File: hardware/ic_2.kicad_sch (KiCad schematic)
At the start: 24 parts, among them IC3 BTS722204ESAXUMA1

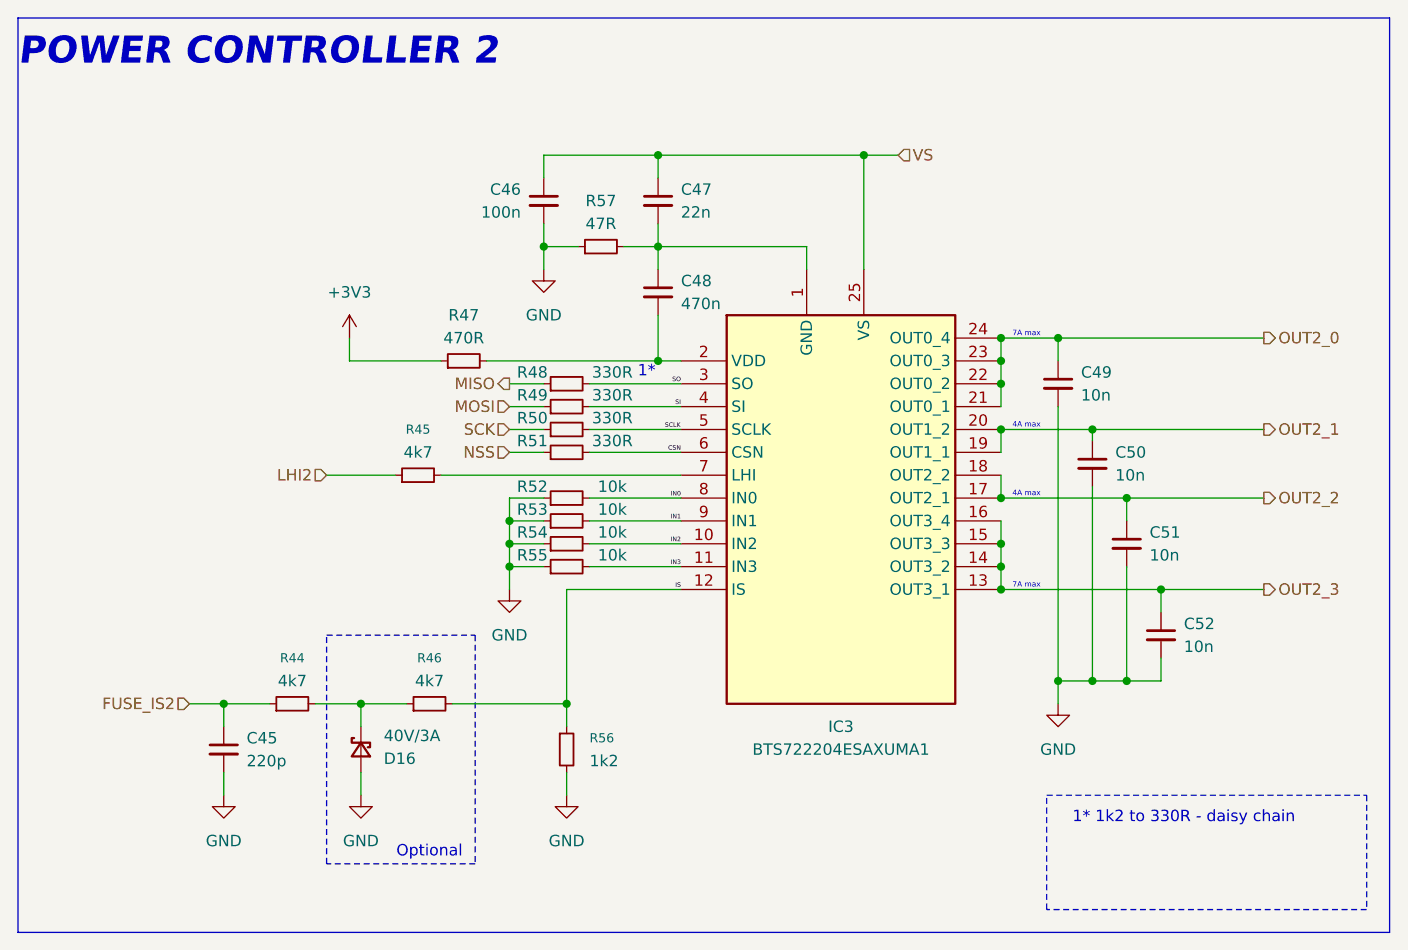
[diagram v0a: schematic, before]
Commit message: new pcb layout & can coppied from steeringwheel
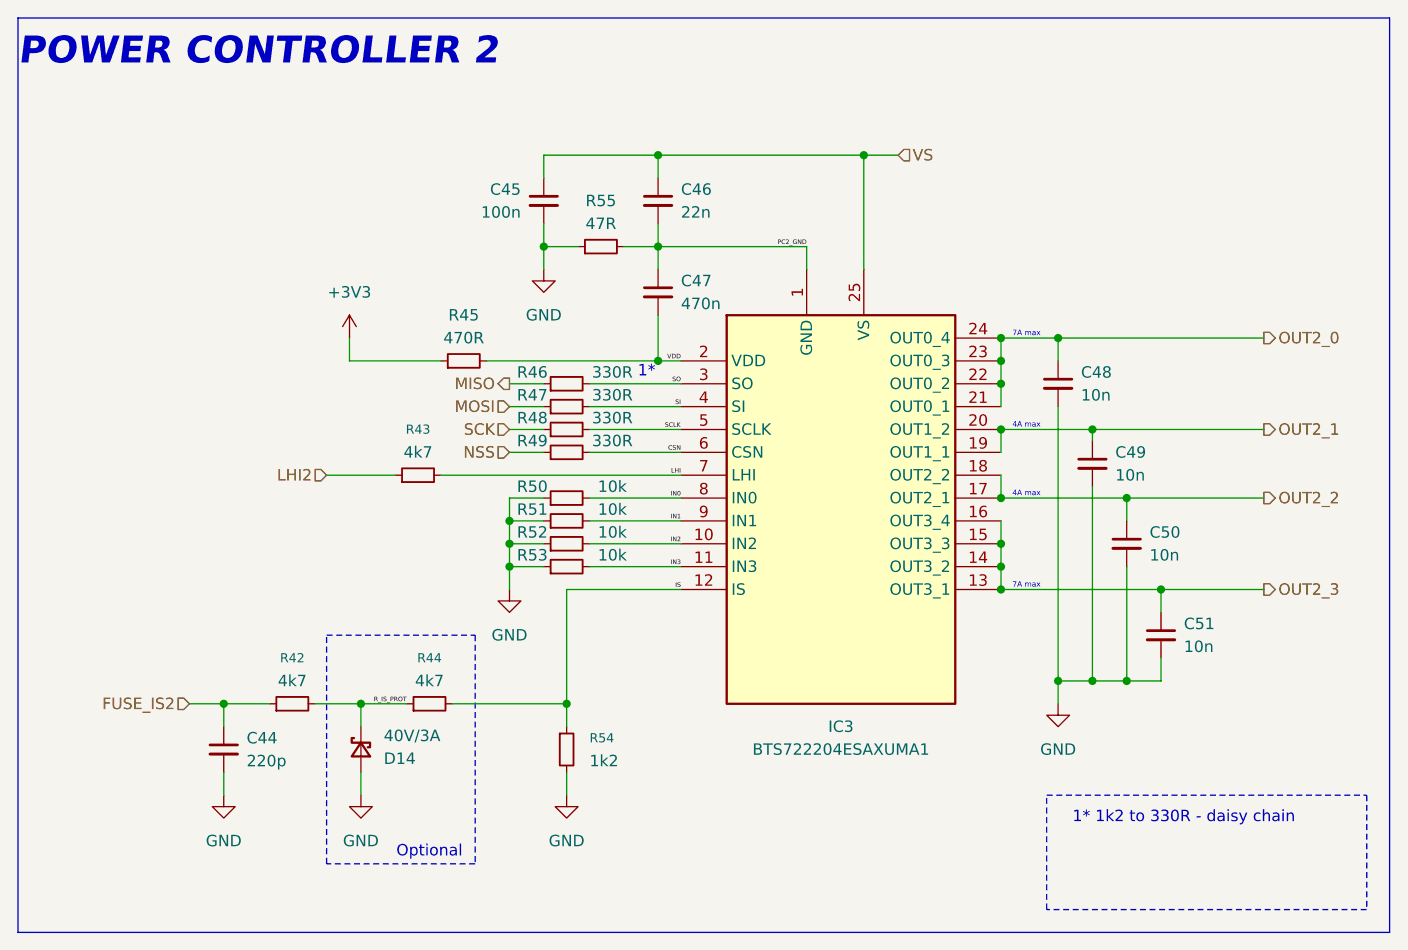
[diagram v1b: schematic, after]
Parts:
- renumbered C45 to C44, C46 to C45, C47 to C46, C48 to C47, C49 to C48, C50 to C49, C51 to C50, C52 to C51, D16 to D14, R44 to R42, R45 to R43, R46 to R44, R47 to R45, R48 to R46, R49 to R47, R50 to R48, R51 to R49, R52 to R50, R53 to R51, R54 to R52, R55 to R53, R56 to R54, R57 to R55
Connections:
- net PC2_GND: now reaches C46.2, C47.1, IC3.1 (GND), R55.2
- net VDD: now reaches C47.2, IC3.2 (VDD), R45.2
- net LHI: now reaches IC3.7 (LHI), R43.2
- net R_IS_PROT: now reaches D14.1 (K), R42.2, R44.1
